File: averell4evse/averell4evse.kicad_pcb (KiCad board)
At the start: 2 copper layers, 91 x 78 mm, 35 parts, among them J1 Conn_01x16, J2 Conn_01x12, J3 Conn_01x04, U1 KT2520K-T, U2 NFCv4, U3 TLC5957RTQ, U4 74AUC1G126, U5 touch_sensor

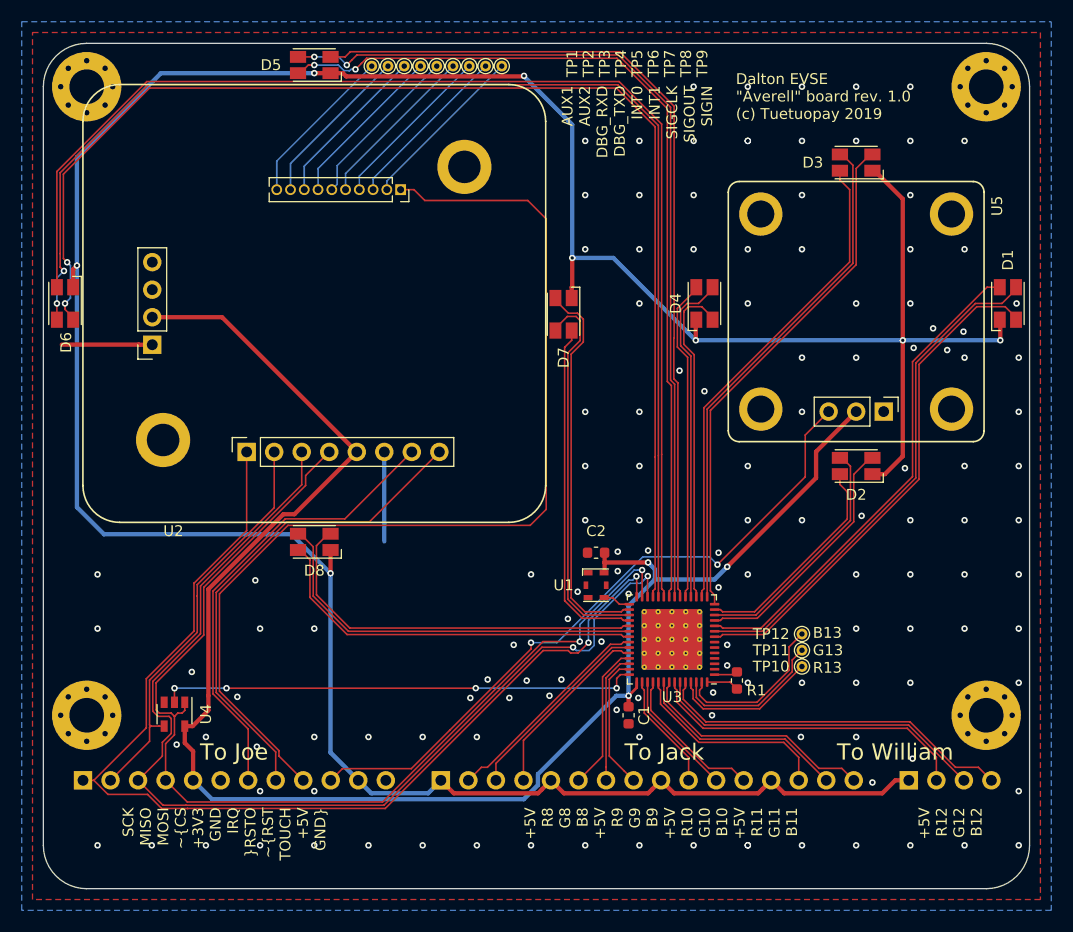
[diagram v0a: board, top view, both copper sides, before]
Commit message: averell/pcb: Re-route LEDs with three per side
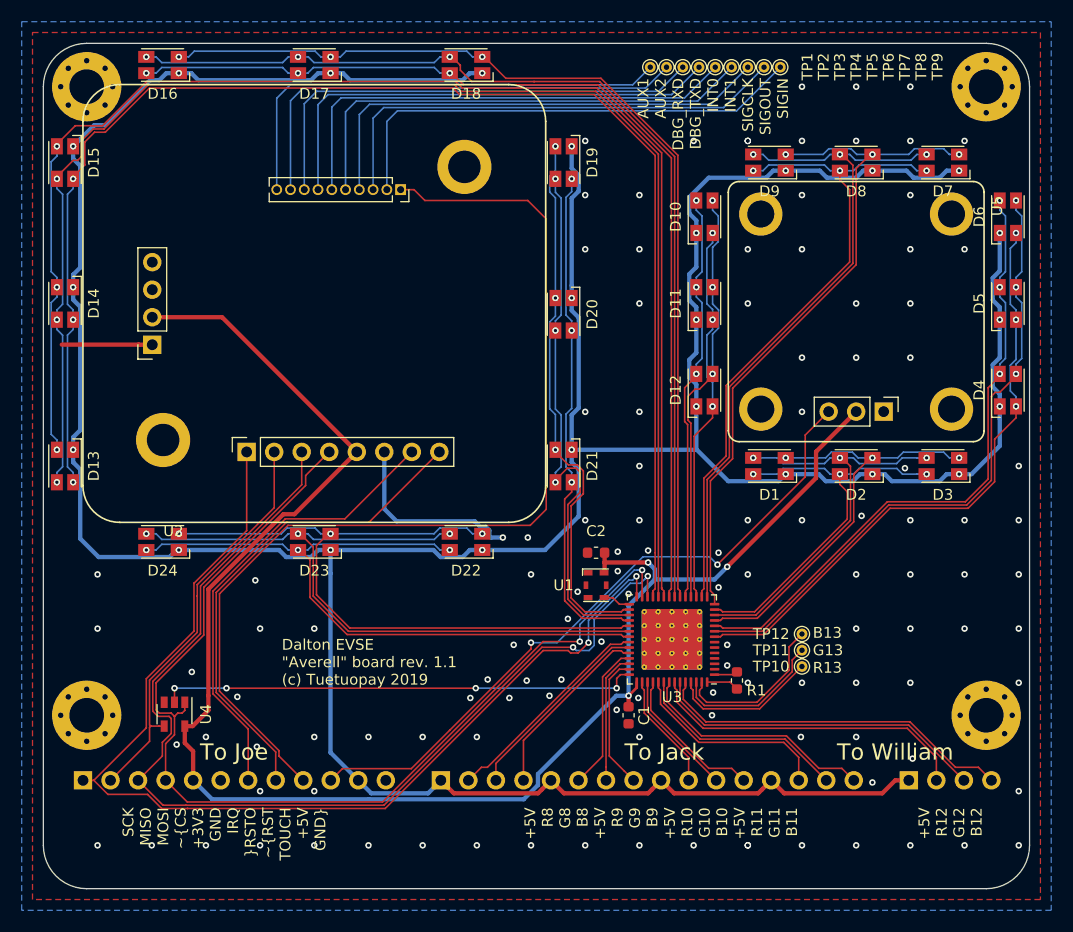
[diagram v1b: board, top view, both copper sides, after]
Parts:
- added D10: ASMB-MTB0-0A3A2, ma4evse:LED_Avago_PLCC4_3.2x2.8mm_CW, F.Cu at (136.0, 67.0)
- added D11: ASMB-MTB0-0A3A2, ma4evse:LED_Avago_PLCC4_3.2x2.8mm_CW, F.Cu at (136.0, 75.0)
- added D12: ASMB-MTB0-0A3A2, ma4evse:LED_Avago_PLCC4_3.2x2.8mm_CW, F.Cu at (136.0, 83.0)
- added D13: ASMB-MTB0-0A3A2, ma4evse:LED_Avago_PLCC4_3.2x2.8mm_CW, F.Cu at (77.0, 90.0)
- added D14: ASMB-MTB0-0A3A2, ma4evse:LED_Avago_PLCC4_3.2x2.8mm_CW, F.Cu at (77.0, 75.0)
- added D15: ASMB-MTB0-0A3A2, ma4evse:LED_Avago_PLCC4_3.2x2.8mm_CW, F.Cu at (77.0, 62.0)
- added D16: ASMB-MTB0-0A3A2, ma4evse:LED_Avago_PLCC4_3.2x2.8mm_CW, F.Cu at (86.0, 53.0)
- added D17: ASMB-MTB0-0A3A2, ma4evse:LED_Avago_PLCC4_3.2x2.8mm_CW, F.Cu at (100.0, 53.0)
- added D18: ASMB-MTB0-0A3A2, ma4evse:LED_Avago_PLCC4_3.2x2.8mm_CW, F.Cu at (114.0, 53.0)
- added D19: ASMB-MTB0-0A3A2, ma4evse:LED_Avago_PLCC4_3.2x2.8mm_CW, F.Cu at (123.0, 62.0)
- added D20: ASMB-MTB0-0A3A2, ma4evse:LED_Avago_PLCC4_3.2x2.8mm_CW, F.Cu at (123.0, 76.0)
- added D21: ASMB-MTB0-0A3A2, ma4evse:LED_Avago_PLCC4_3.2x2.8mm_CW, F.Cu at (123.0, 90.0)
- added D22: ASMB-MTB0-0A3A2, ma4evse:LED_Avago_PLCC4_3.2x2.8mm_CW, F.Cu at (114.0, 97.0)
- added D23: ASMB-MTB0-0A3A2, ma4evse:LED_Avago_PLCC4_3.2x2.8mm_CW, F.Cu at (100.0, 97.0)
- added D24: ASMB-MTB0-0A3A2, ma4evse:LED_Avago_PLCC4_3.2x2.8mm_CW, F.Cu at (86.0, 97.0)
- added D9: ASMB-MTB0-0A3A2, ma4evse:LED_Avago_PLCC4_3.2x2.8mm_CW, F.Cu at (142.0, 62.0)
- moved D6 87.4 mm to (164.0, 67.0), turned to 90 degrees
- moved D5 67.7 mm to (164.0, 75.0), turned to 90 degrees
- moved D8 61.0 mm to (150.0, 62.0)
- moved D7 37.7 mm to (158.0, 62.0), turned to 180 degrees
- moved D3 29.1 mm to (158.0, 90.0)
- moved D4 29.1 mm to (164.0, 83.0)
- moved D1 26.6 mm to (142.0, 90.0), turned to 180 degrees
- moved TP1 25.7 mm to (131.0, 53.2)
- moved TP2 25.7 mm to (132.5, 53.2)
- moved TP3 25.7 mm to (134.0, 53.2)
- moved TP4 25.7 mm to (135.5, 53.2)
- moved TP5 25.7 mm to (137.0, 53.2)
- moved TP6 25.7 mm to (138.5, 53.2)
- moved TP7 25.7 mm to (140.0, 53.2)
- moved TP8 25.7 mm to (141.5, 53.2)
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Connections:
- D1 pad 2: /B0 -> /B1
- D1 pad 3: /G0 -> /G1
- D1 pad 4: /R0 -> /R1
- D3 pad 2: /B2 -> /B1
- D3 pad 3: /G2 -> /G1
- D3 pad 4: /R2 -> /R1
- D4 pad 2: /B3 -> /B0
- D4 pad 3: /G3 -> /G0
- D4 pad 4: /R3 -> /R0
- D5 pad 2: /B4 -> /B0
- D5 pad 3: /G4 -> /G0
- D5 pad 4: /R4 -> /R0
- D6 pad 2: /B5 -> /B0
- D6 pad 3: /G5 -> /G0
- D6 pad 4: /R5 -> /R0
- D7 pad 2: /B6 -> /B2
- D7 pad 3: /G6 -> /G2
- D7 pad 4: /R6 -> /R2
- D8 pad 2: /B7 -> /B2
- D8 pad 3: /G7 -> /G2
- D8 pad 4: /R7 -> /R2
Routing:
- net +5V: track 283.0 -> 357.8 mm, vias 8 -> 24
- net Net-(TP5-Pad1): track 15.4 -> 44.5 mm
- net Net-(TP4-Pad1): track 15.3 -> 44.4 mm
- net Net-(TP2-Pad1): track 15.1 -> 44.2 mm
- net Net-(TP1-Pad1): track 15.0 -> 44.1 mm
- net Net-(TP3-Pad1): track 15.2 -> 44.2 mm
- net Net-(TP6-Pad1): track 15.5 -> 44.5 mm
- net Net-(TP7-Pad1): track 15.6 -> 44.6 mm
- net Net-(TP8-Pad1): track 15.7 -> 44.6 mm
- net Net-(TP9-Pad1): track 15.8 -> 44.7 mm
- net /G7: track 37.0 -> 65.8 mm, vias 0 -> 3
- net /B7: track 35.9 -> 64.8 mm, vias 0 -> 3
- net /R7: track 36.5 -> 65.4 mm, vias 0 -> 3
- net /R1: track 23.3 -> 40.2 mm, vias 0 -> 3
- net /R2: track 48.0 -> 64.8 mm, vias 0 -> 3
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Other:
- board text added: "Dalton EVSE "Averell" board rev. 1.1 (c) Tuetuopay 2019"
- board text removed: "Dalton EVSE "Averell" board rev. 1.0 (c) Tuetuopay 2019"

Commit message: averell: Replace test pads with 0.1" pin headers
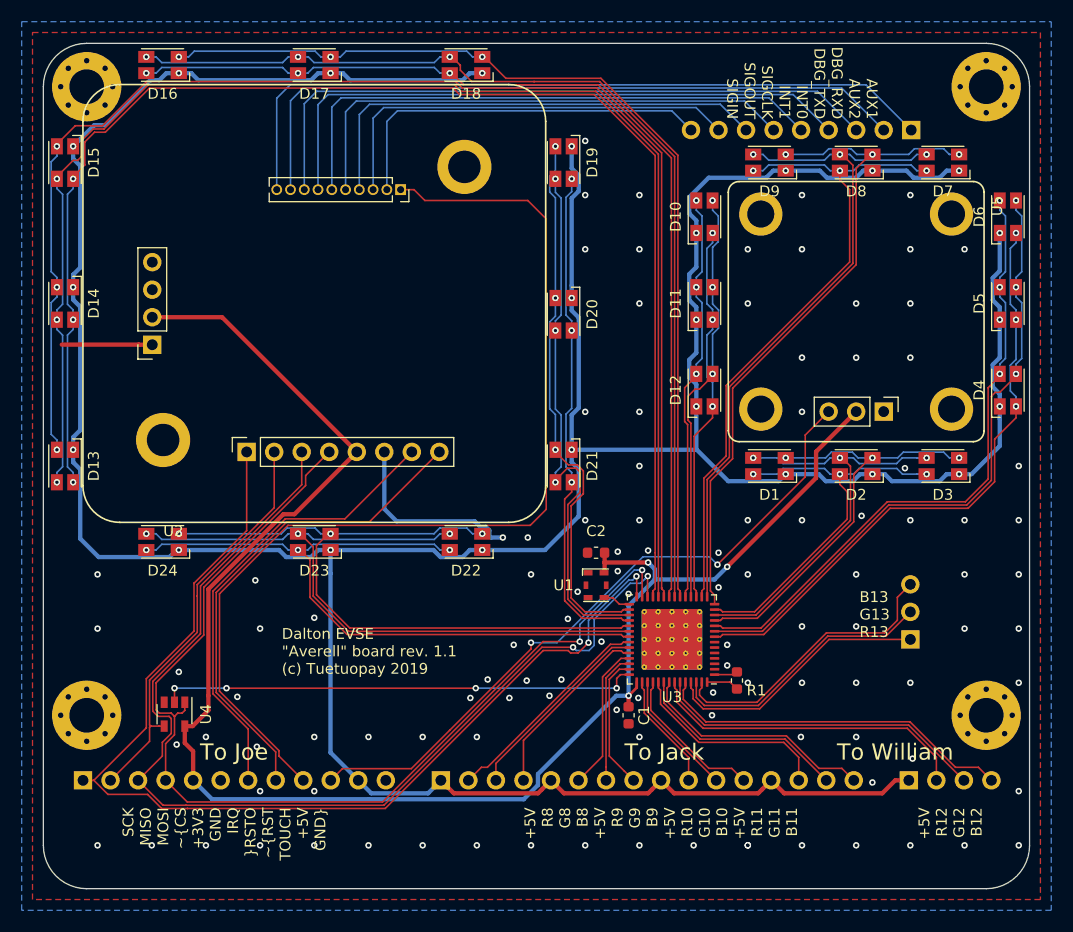
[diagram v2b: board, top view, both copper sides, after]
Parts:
- removed TP1: AUX1, TestPoint:TestPoint_THTPad_D1.0mm_Drill0.5mm
- removed TP10: R13, TestPoint:TestPoint_THTPad_D1.0mm_Drill0.5mm
- removed TP11: G13, TestPoint:TestPoint_THTPad_D1.0mm_Drill0.5mm
- removed TP12: B13, TestPoint:TestPoint_THTPad_D1.0mm_Drill0.5mm
- removed TP2: AUX2, TestPoint:TestPoint_THTPad_D1.0mm_Drill0.5mm
- removed TP3: DBG_RXD, TestPoint:TestPoint_THTPad_D1.0mm_Drill0.5mm
- removed TP4: DBG_TXD, TestPoint:TestPoint_THTPad_D1.0mm_Drill0.5mm
- removed TP5: INT0, TestPoint:TestPoint_THTPad_D1.0mm_Drill0.5mm
- removed TP6: INT1, TestPoint:TestPoint_THTPad_D1.0mm_Drill0.5mm
- removed TP7: SIGCLK, TestPoint:TestPoint_THTPad_D1.0mm_Drill0.5mm
- removed TP8: SIGOUT, TestPoint:TestPoint_THTPad_D1.0mm_Drill0.5mm
- removed TP9: SIGIN, TestPoint:TestPoint_THTPad_D1.0mm_Drill0.5mm
- added J4: Conn_01x03, Connector_PinHeader_2.54mm:PinHeader_1x03_P2.54mm_Horizontal, B.Cu at (155.0, 106.0)
- added J5: Conn_01x09, Connector_PinHeader_2.54mm:PinHeader_1x09_P2.54mm_Horizontal, B.Cu at (155.1, 59.0)
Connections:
- U2 pad 14: Net-(TP9-Pad1) -> /SIGIN
- U2 pad 15: Net-(TP8-Pad1) -> /SIGOUT
- U2 pad 16: Net-(TP7-Pad1) -> /SIGCLK
- U2 pad 17: Net-(TP6-Pad1) -> /INT1
- U2 pad 18: Net-(TP5-Pad1) -> /INT0
- U2 pad 19: Net-(TP4-Pad1) -> /DBG_TXD
- U2 pad 20: Net-(TP3-Pad1) -> /DBG_RXD
- U2 pad 21: Net-(TP2-Pad1) -> /AUX2
- U2 pad 22: Net-(TP1-Pad1) -> /AUX1
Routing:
- net /AUX1: track 0.00 -> 69.2 mm
- net /AUX2: track 0.00 -> 65.0 mm
- net /DBG_RXD: track 0.00 -> 60.8 mm
- net /DBG_TXD: track 0.00 -> 56.7 mm
- net /INT0: track 0.00 -> 52.5 mm
- net /INT1: track 0.00 -> 48.2 mm
- net Net-(TP9-Pad1): track 44.7 -> 0.00 mm
- net Net-(TP8-Pad1): track 44.6 -> 0.00 mm
- net Net-(TP7-Pad1): track 44.6 -> 0.00 mm
- net Net-(TP5-Pad1): track 44.5 -> 0.00 mm
- net Net-(TP6-Pad1): track 44.5 -> 0.00 mm
- net Net-(TP4-Pad1): track 44.4 -> 0.00 mm
- net Net-(TP3-Pad1): track 44.2 -> 0.00 mm
- net Net-(TP2-Pad1): track 44.2 -> 0.00 mm
- net Net-(TP1-Pad1): track 44.1 -> 0.00 mm
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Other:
- board text added: "AUX1 AUX2 DBG_RXD DBG_TXD INT0 INT1 SIGCLK SIGOUT"
- board text added: "SIGIN"

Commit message: averell/pcb: Fix some silkscreen labels placement
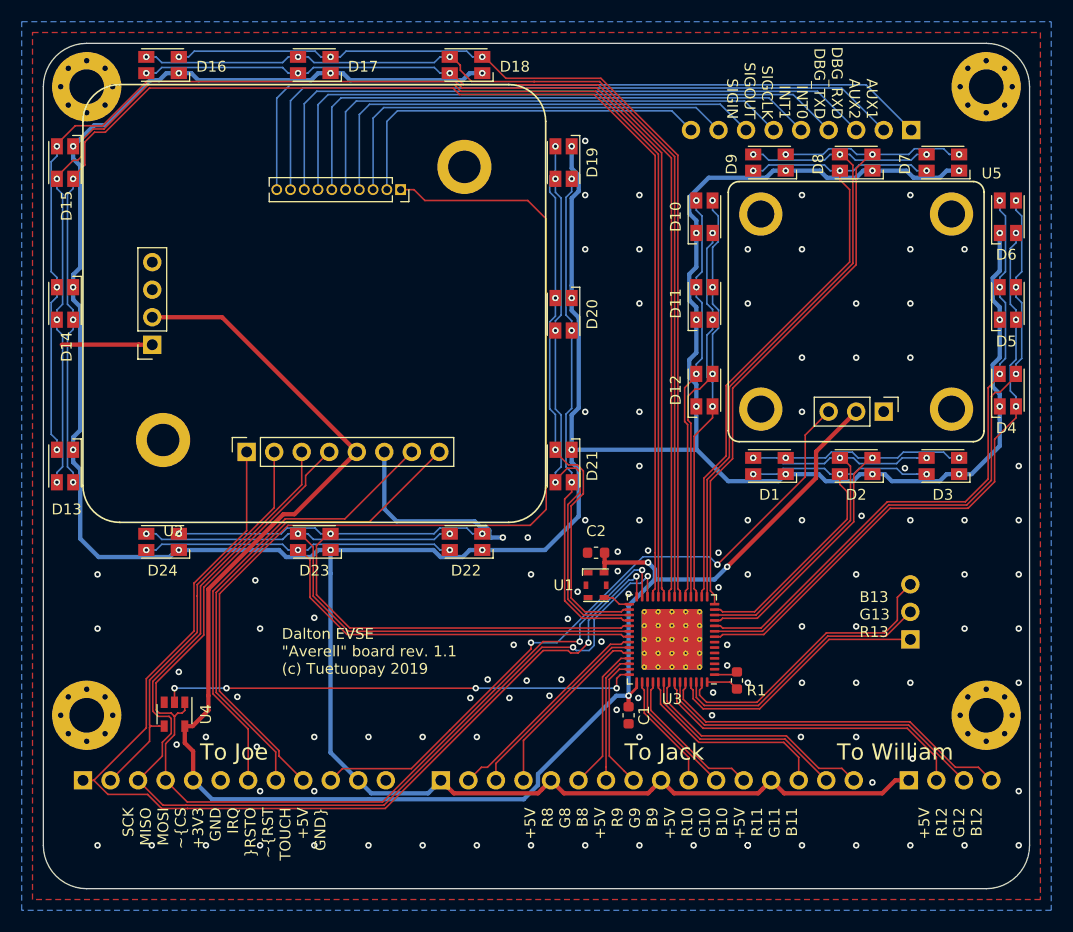
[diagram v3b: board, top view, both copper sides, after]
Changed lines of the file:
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@@
     (tags "LED Avago PLCC-4 ASMB-MTB0-0A3A2")
     (attr smd)
-    (fp_text reference D18 (at 0 -2.65 180) (layer F.SilkS)
+    (fp_text reference D18 (at -4.5 -0.15 180) (layer F.SilkS)
       (effects (font (size 1 1) (thickness 0.15)))
     )
@@
     (tags "LED Avago PLCC-4 ASMB-MTB0-0A3A2")
     (attr smd)
-    (fp_text reference D17 (at 0 -2.65 180) (layer F.SilkS)
+    (fp_text reference D17 (at -4.5 -0.15 180) (layer F.SilkS)
       (effects (font (size 1 1) (thickness 0.15)))
     )
@@
     (tags "LED Avago PLCC-4 ASMB-MTB0-0A3A2")
     (attr smd)
-    (fp_text reference D16 (at 0 -2.65 180) (layer F.SilkS)
+    (fp_text reference D16 (at -4.5 -0.15 180) (layer F.SilkS)
       (effects (font (size 1 1) (thickness 0.15)))
     )
@@
     (tags "LED Avago PLCC-4 ASMB-MTB0-0A3A2")
     (attr smd)
-    (fp_text reference D15 (at 0 -2.65 270) (layer F.SilkS)
+    (fp_text reference D15 (at 4 -0.15 270) (layer F.SilkS)
       (effects (font (size 1 1) (thickness 0.15)))
     )
@@
     (tags "LED Avago PLCC-4 ASMB-MTB0-0A3A2")
     (attr smd)
-    (fp_text reference D14 (at 0 -2.65 270) (layer F.SilkS)
+    (fp_text reference D14 (at 4 -0.15 270) (layer F.SilkS)
       (effects (font (size 1 1) (thickness 0.15)))
     )
@@
     (tags "LED Avago PLCC-4 ASMB-MTB0-0A3A2")
     (attr smd)
-    (fp_text reference D13 (at 0 -2.65 270) (layer F.SilkS)
+    (fp_text reference D13 (at 4 -0.15) (layer F.SilkS)
       (effects (font (size 1 1) (thickness 0.15)))
     )
@@
     (tags "LED Avago PLCC-4 ASMB-MTB0-0A3A2")
     (attr smd)
-    (fp_text reference D9 (at 0 -2.65 180) (layer F.SilkS)
+    (fp_text reference D9 (at 3.5 -0.15 270) (layer F.SilkS)
       (effects (font (size 1 1) (thickness 0.15)))
     )
@@
     (tags "LED Avago PLCC-4 ASMB-MTB0-0A3A2")
     (attr smd)
-    (fp_text reference D8 (at 0 -2.65 180) (layer F.SilkS)
+    (fp_text reference D8 (at 3.5 -0.15 270) (layer F.SilkS)
       (effects (font (size 1 1) (thickness 0.15)))
     )
@@
     (tags "LED Avago PLCC-4 ASMB-MTB0-0A3A2")
     (attr smd)
-    (fp_text reference D7 (at 0 -2.65 180) (layer F.SilkS)
+    (fp_text reference D7 (at 3.5 -0.15 270) (layer F.SilkS)
       (effects (font (size 1 1) (thickness 0.15)))
     )
@@
     (tags "LED Avago PLCC-4 ASMB-MTB0-0A3A2")
     (attr smd)
-    (fp_text reference D6 (at 0 -2.65 90) (layer F.SilkS)
+    (fp_text reference D6 (at -3.5 -0.15 180) (layer F.SilkS)
       (effects (font (size 1 1) (thickness 0.15)))
     )
@@
     (tags "LED Avago PLCC-4 ASMB-MTB0-0A3A2")
     (attr smd)
-    (fp_text reference D5 (at 0 -2.65 90) (layer F.SilkS)
+    (fp_text reference D5 (at -3.5 -0.15 180) (layer F.SilkS)
       (effects (font (size 1 1) (thickness 0.15)))
     )
@@
     (tags "LED Avago PLCC-4 ASMB-MTB0-0A3A2")
     (attr smd)
-    (fp_text reference D4 (at 0 -2.65 90) (layer F.SilkS)
+    (fp_text reference D4 (at -3.5 -0.15 180) (layer F.SilkS)
       (effects (font (size 1 1) (thickness 0.15)))
     )
@@
   (module ma4evse:touch_sensor (layer F.Cu)
     (at 150 75 270)
-    (fp_text reference U5 (at -9 -13 270) (layer F.SilkS)
+    (fp_text reference U5 (at -12 -12.5) (layer F.SilkS)
       (effects (font (size 1 1) (thickness 0.15)))
     )
@@
     (zone_connect 2)
     (attr smd)
-    (fp_text reference U3 (at 0 -5.32 180) (layer F.SilkS)
-      (effects (font (size 1 1) (thickness 0.15)))
-    )
+    (fp_text reference U3 (at 0 -5.5 180) (layer F.SilkS)
+      (effects (font (size 1 1) (thickness 0.15)))
+    )
